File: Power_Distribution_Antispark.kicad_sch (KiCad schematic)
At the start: 88 parts, among them J1 STM Signal Conn, J5 +48V Battery Conn, J6 Motor Conn, Q1 BUK9M42-60EX, Q2 G20P06K, Q3 BUK9M42-60EX, Q4 G20P06K, U1 74LVC1G14GW_125, U2 TPP60308-ES1R-S, U3 TPP60308-ES1R-S, U4 LM331AU-S5TR, U5 TLV74033PDBVR, U8 INA181A3IDBVR

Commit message: final schematic
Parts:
- added R29: 1.1K, Resistor_SMD:R_0201_0603Metric, symbol Device:R_Small_US
- added R30: 1.3K, Resistor_SMD:R_0201_0603Metric, symbol Device:R_Small_US
- R15: value DTO025C100R0JTE3 -> TPAL0263F100RK9; footprint CustomFootprintLibrary:RES_DTO025_VIS -> Package_TO_SOT_SMD:TO-263-3_TabPin4
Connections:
- net GND: now also R30.2
- net PreChargeSense: no longer R32.1
- net PreChargeSenseEnd: now also R29.1, R30.1; no longer D9.2 (A), R32.2
- net at R15.2, R16.2, R33.2: now also R32.1
- new net: D9.2 (A), R29.2, R32.2
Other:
- note added: "I = 0.5A"
- moved on the sheet: R33, R34

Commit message: final schematic
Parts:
- removed C15: 47uF, Capacitor_SMD:C_0201_0603Metric, symbol Device:C_Small
- removed C22, C27: 1uF, Capacitor_SMD:C_0201_0603Metric, symbol Device:C_Small
- removed C3: 2.2uF, Capacitor_SMD:C_0805_2012Metric, symbol Device:C_Small
- removed C8: 39pF, Capacitor_SMD:C_0201_0603Metric, symbol Device:C_Small
- removed R11, R23, R29: 1.1K, Resistor_SMD:R_0201_0603Metric, symbol Device:R_Small_US
- removed R13: 10K, Resistor_SMD:R_0201_0603Metric, symbol Device:R_Small_US
- removed R34: 1.3K, Resistor_SMD:R_0201_0603Metric, symbol Device:R_Small_US
- added C18: 47uF, Capacitor_SMD:C_1206_3216Metric, symbol Device:C_Small
- added C21, C7: 100nF, Capacitor_SMD:C_0603_1608Metric, symbol Device:C_Small
- added C23: 1uF, Capacitor_SMD:C_0603_1608Metric, symbol Device:C_Small
- added C5: 2.2uF, Capacitor_SMD:C_0603_1608Metric, symbol Device:C_Small
- added R15, R20: 2.2K, Resistor_SMD:R_0603_1608Metric, symbol Device:R_Small_US
- added R22: 11K, Resistor_SMD:R_0603_1608Metric, symbol Device:R_Small_US
- added R31: 13K, Resistor_SMD:R_0603_1608Metric, symbol Device:R_Small_US
- added R47: 20K, Resistor_SMD:R_0603_1608Metric, symbol Device:R_Small_US
- C1: renamed from C20; footprint Capacitor_SMD:C_0201_0603Metric -> Capacitor_SMD:C_0603_1608Metric
- C10: value 6.8nF -> 39pF; footprint Capacitor_SMD:C_0201_0603Metric -> Capacitor_SMD:C_0603_1608Metric
- C11: renamed from C7; footprint Capacitor_SMD:C_0201_0603Metric -> Capacitor_SMD:C_0603_1608Metric
- C12: value 100nF -> 6.8nF; footprint Capacitor_SMD:C_0201_0603Metric -> Capacitor_SMD:C_0603_1608Metric
- C13: renamed from C9; footprint Capacitor_SMD:C_0201_0603Metric -> Capacitor_SMD:C_0603_1608Metric
- C14: value 47uF -> 100nF; footprint Capacitor_SMD:C_0201_0603Metric -> Capacitor_SMD:C_0603_1608Metric
- C15: renamed from C11; footprint Capacitor_SMD:C_0201_0603Metric -> Capacitor_SMD:C_0603_1608Metric
- C16: footprint Capacitor_SMD:C_0201_0603Metric -> Capacitor_SMD:C_1206_3216Metric
- C17: renamed from C13; footprint Capacitor_SMD:C_0201_0603Metric -> Capacitor_SMD:C_1206_3216Metric
- C19: value 100nF -> 47uF; footprint Capacitor_SMD:C_0201_0603Metric -> Capacitor_SMD:C_1206_3216Metric
- C2, C4: footprint Capacitor_SMD:C_0805_2012Metric -> Capacitor_SMD:C_0603_1608Metric
- C20: renamed from C17; footprint Capacitor_SMD:C_0201_0603Metric -> Capacitor_SMD:C_0603_1608Metric
- C22: renamed from C18; footprint Capacitor_SMD:C_0201_0603Metric -> Capacitor_SMD:C_0603_1608Metric
- C3: renamed from C1; footprint Capacitor_SMD:C_0805_2012Metric -> Capacitor_SMD:C_0603_1608Metric
- C6: value 100nF -> 1uF; footprint Capacitor_SMD:C_0201_0603Metric -> Capacitor_SMD:C_0603_1608Metric
- C8: renamed from C5; footprint Capacitor_SMD:C_0201_0603Metric -> Capacitor_SMD:C_0603_1608Metric
- C9: renamed from C24; footprint Capacitor_SMD:C_0201_0603Metric -> Capacitor_SMD:C_0603_1608Metric
- R1, R2, R3, R4: footprint Resistor_SMD:R_0201_0603Metric -> Resistor_SMD:R_0603_1608Metric
- R10: renamed from R5; footprint Resistor_SMD:R_0201_0603Metric -> Resistor_SMD:R_0603_1608Metric
- R11: renamed from R8; footprint Resistor_SMD:R_0201_0603Metric -> Resistor_SMD:R_0603_1608Metric
- R12: renamed from R7; footprint Resistor_SMD:R_0201_0603Metric -> Resistor_SMD:R_0603_1608Metric
- R13: renamed from R9; footprint Resistor_SMD:R_0201_0603Metric -> Resistor_SMD:R_0603_1608Metric
- R14: renamed from R10; footprint Resistor_SMD:R_0201_0603Metric -> Resistor_SMD:R_0603_1608Metric
- R16: value 10K -> 20K; footprint Resistor_SMD:R_0201_0603Metric -> Resistor_SMD:R_0603_1608Metric
- R17: renamed from R14; footprint Resistor_SMD:R_0201_0603Metric -> Resistor_SMD:R_0603_1608Metric
- R18: renamed from R12; footprint Resistor_SMD:R_0201_0603Metric -> Resistor_SMD:R_0603_1608Metric
- R19: renamed from R15; footprint Package_TO_SOT_SMD:TO-263-3_TabPin4 -> Package_TO_SOT_SMD:TO-263-2
- R23: renamed from R33; value 1.1K -> 11K; footprint Resistor_SMD:R_0201_0603Metric -> Resistor_SMD:R_0603_1608Metric
- R24: renamed from R20; footprint Resistor_SMD:R_0201_0603Metric -> Resistor_SMD:R_0603_1608Metric
- R25: renamed from R21; footprint Resistor_SMD:R_0201_0603Metric -> Resistor_SMD:R_0603_1608Metric
- R26: renamed from R22; footprint Resistor_SMD:R_0201_0603Metric -> Resistor_SMD:R_0603_1608Metric
- R27: renamed from R17; footprint Resistor_SMD:R_0201_0603Metric -> Resistor_SMD:R_0603_1608Metric
- R28: renamed from R18; footprint Resistor_SMD:R_0201_0603Metric -> Resistor_SMD:R_0603_1608Metric
- R29: renamed from R19; footprint Resistor_SMD:R_0201_0603Metric -> Resistor_SMD:R_0603_1608Metric
- R30: value 1.3K -> 13K; footprint Resistor_SMD:R_0201_0603Metric -> Resistor_SMD:R_0603_1608Metric
- R33: renamed from R24; footprint Resistor_SMD:R_0201_0603Metric -> Resistor_SMD:R_0603_1608Metric
- R34: renamed from R31; footprint Resistor_SMD:R_0201_0603Metric -> Resistor_SMD:R_0603_1608Metric
- R35: renamed from R27; footprint Resistor_SMD:R_0201_0603Metric -> Resistor_SMD:R_0603_1608Metric
- R36: renamed from R28; footprint Resistor_SMD:R_0201_0603Metric -> Resistor_SMD:R_0603_1608Metric
- R37: renamed from R25; footprint Resistor_SMD:R_0201_0603Metric -> Resistor_SMD:R_0603_1608Metric
- R38: renamed from R26; footprint Resistor_SMD:R_0201_0603Metric -> Resistor_SMD:R_0603_1608Metric
- R5: renamed from R36; footprint Resistor_SMD:R_0201_0603Metric -> Resistor_SMD:R_0603_1608Metric
- R6: renamed from R46; footprint Resistor_SMD:R_0201_0603Metric -> Resistor_SMD:R_0603_1608Metric
- R7: renamed from R35; footprint Resistor_SMD:R_0201_0603Metric -> Resistor_SMD:R_0603_1608Metric
- R8: renamed from R45; footprint Resistor_SMD:R_0201_0603Metric -> Resistor_SMD:R_0603_1608Metric
- R9: renamed from R6; footprint Resistor_SMD:R_0201_0603Metric -> Resistor_SMD:R_0603_1608Metric
- renumbered D2 to D1, D7 to D10, D9 to D11, D1 to D2, D12 to D3, D3 to D5, D5 to D6, D6 to D7, D13 to D8, D8 to D9, J5 to J2, J6 to J3, L2 to L1, L1 to L2, R32 to R21, U5 to U1, U1 to U2, U2 to U4, U4 to U5, U8 to U6
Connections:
- net +12V: now also C19.1
- net +3V3: now also C6.1
- net +5V: now also C18.1, C23.1; no longer C14.1, C6.1, C8.1, R5.1, R6.1, R7.1, R8.1, U3.3 (EN), U4.3 (EN)
- net GND: now also C12.2, C18.2, C21.2, C23.2, C5.2, C7.2, R15.1, R20.1, R31.2; no longer C14.2, C2.2
- net PreChargeSense: now also R30.1
- net PreChargeSenseEnd: now also R22.1, R31.1; no longer R30.1
- net V_S_5V_Output: now also C21.1; no longer C19.1
- net at U5.1 (IN-): now also R15.2, R47.2
- net at R9.1, U3.6 (COMP): now also C10.1
- net at R9.2: now also C12.1; no longer C10.1
- net at R21.1, R23.2: now also R16.1, R19.3; no longer R16.2, R19.2
- net at D9.1 (K), L1.1, U3.8 (SW): now also C14.1; no longer C12.1
- net at R17.2: now also C14.2; no longer C12.2
- net at C3.1, F2.2, R8.2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: now also C4.1
- net at R33.1, U5.3 (IN+): now also R16.2, R20.2; no longer R16.1
- net at Q4.2 (D), R19.1: now also R47.1
- net at F3.2, R7.2, U3.2 (VIN): now also C5.1; no longer C2.1, C4.1
- net at D11.2 (A), R21.2: now also R22.2
- net C_Sense_12V1 renamed C_Sense_12V_1
- net C_Sense_12V2 renamed C_Sense_12V_2
- net C_Sense_12V3 renamed C_Sense_12V_3
- net C_Sense_5V1 renamed C_Sense_5V_1
- net C_Sense_5V2 renamed C_Sense_5V_2
- net C_Sense_5V3 renamed C_Sense_5V_3
- new net: C8.1, R6.1, R8.1, U4.3 (EN)
- new net: C7.1, R5.1, R7.1, U3.3 (EN)

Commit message: final schematic
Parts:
- R5, R6: value 1.5K -> 3K
- R7, R8: value 10.5K -> 21K
- renumbered C3 to C2, C2 to C3, R47 to R16, R16 to R20, R20 to R30, R30 to R31, R31 to R32
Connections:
- net GND: now also C3.2
- net at C3.1: now also C5.1, F3.2, R7.2, U3.2 (VIN)

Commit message: damir review
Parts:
- removed D6: MBRD20100, Package_TO_SOT_SMD:TO-252-3_TabPin2, symbol Diode:1N4148WT
- removed R22, R23: 11K, Resistor_SMD:R_0603_1608Metric, symbol Device:R_Small_US
- removed R31, R32: 13K, Resistor_SMD:R_0603_1608Metric, symbol Device:R_Small_US
- added H1, H2: MountingHole, MountingHole:MountingHole_2.5mm, symbol Mechanical:MountingHole
- R16: value 20K -> 22K
- R33: value 10K -> 402K
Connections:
- net PreChargeSenseEnd is gone; now on net GND: U6.4 (IN-)
- net +48V: no longer J3.1 (P)
- net GND: now also R21.2; no longer J3.2 (N), J3.SH1 (SHIELD), J3.SH2 (SHIELD)
- net MotorConn: now also J3.1 (P)
- net at F1.2: now also D3.1 (K), D7.1 (K), D8.1 (K), Q2.3 (S), Q4.3 (S), R13.1, R4.1
- net at R19.3, R20.1: now also D11.2 (A); no longer R21.1
- net PreChargeSense: no longer names the net of U6.3 (IN+)
- net PreChargeSense: now also J3.2 (N), J3.SH1 (SHIELD), J3.SH2 (SHIELD), R21.1
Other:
- moved on the sheet: C23, D11, F1, J2, J3, R21, U6

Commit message: final schematic
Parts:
- F1: footprint CustomFootprintLibrary:FUSC6125X279N-0679L9150-05 -> CustomFootprintLibrary:FUSE_0679L9200-05_BEL
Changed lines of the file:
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@@
 			)
 		)
-		(property "Footprint" "CustomFootprintLibrary:FUSC6125X279N-0679L9150-05"
+		(property "Footprint" "CustomFootprintLibrary:FUSE_0679L9200-05_BEL"
 			(at 55.88 39.37 0)
 			(effects
@@
 			)
 		)
-		(property "Datasheet" "https://www.digikey.ca/en/products/detail/bel-fuse-inc/0679L9150-05/5844044"
+		(property "Datasheet" "https://www.digikey.ca/en/products/detail/bel-fuse-inc/0679L9200-05/5844045?s=N4IgTCBcDaIAwDYDsBOAMisc4Fo4FYQBdAXyA"
 			(at 55.88 39.37 0)
 			(effects
@@
 			)
 		)
-		(property "Description" "FUSE BRD MNT 15A 125VAC/VDC 2SMD"
+		(property "Description" "FUSE BRD MNT 20A 125VAC/VDC 2SMD"
 			(at 55.88 39.37 0)
 			(effects

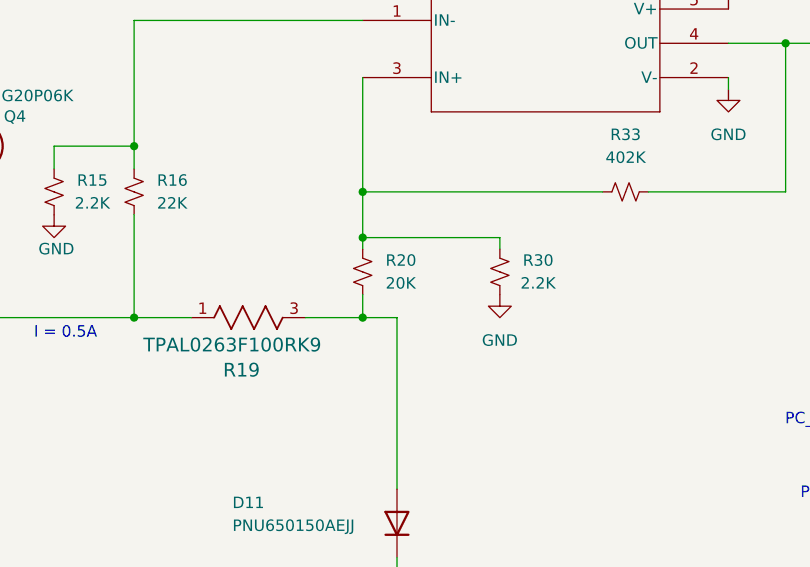
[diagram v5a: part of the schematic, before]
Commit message: tweaked comparator resistor values
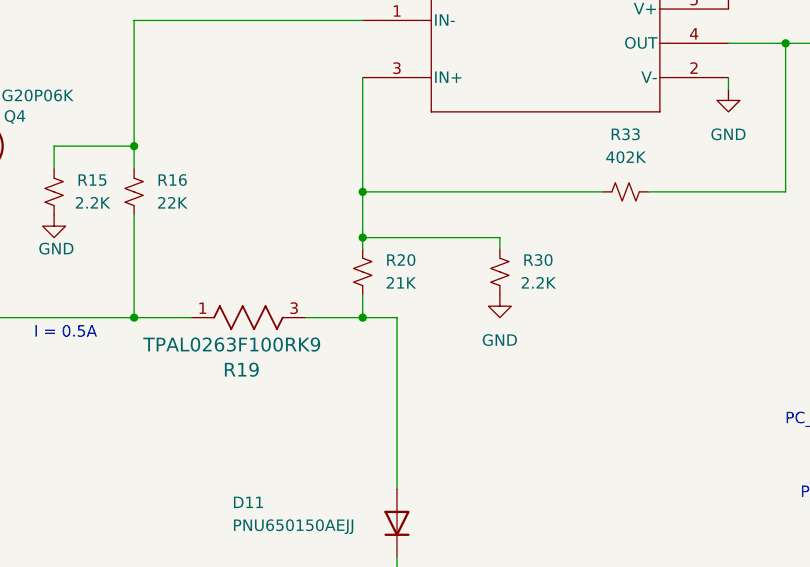
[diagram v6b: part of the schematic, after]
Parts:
- R20: value 20K -> 21K
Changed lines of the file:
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@@
 			)
 		)
-		(property "Value" "20K"
+		(property "Value" "21K"
 			(at 193.04 67.3099 0)
 			(effects
@@
 			)
 		)
-		(property "Datasheet" "https://www.digikey.ca/en/products/detail/stackpole-electronics-inc/RNCF0603BTE20K0/2027042"
+		(property "Datasheet" "https://www.digikey.ca/en/products/detail/stackpole-electronics-inc/RMCF0603FT21K0/1713784"
 			(at 190.5 66.04 0)
 			(effects
@@
 			)
 		)
-		(property "Description" "RES SMD 20K OHM 0.1% 1/6W 0603"
+		(property "Description" "RES 21K OHM 1% 1/10W 0603"
 			(at 190.5 66.04 0)
 			(effects

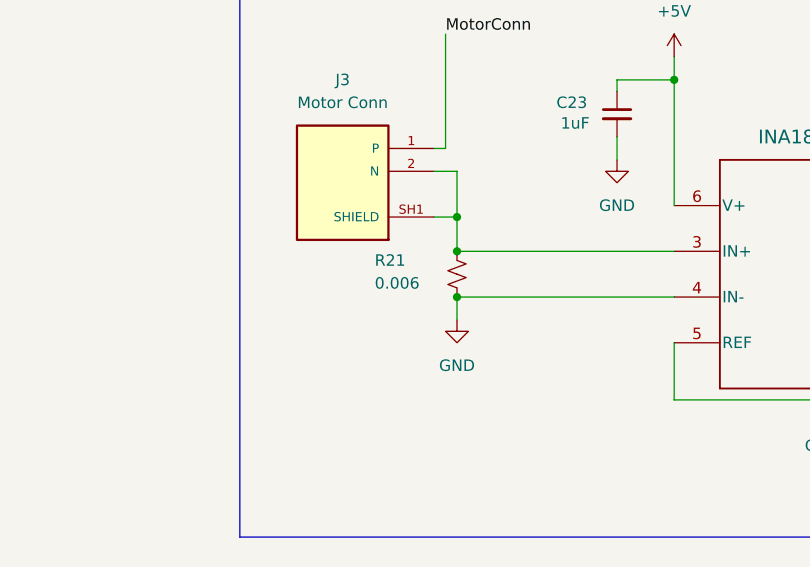
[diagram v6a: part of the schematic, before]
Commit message: tweaked comparator values and shunt
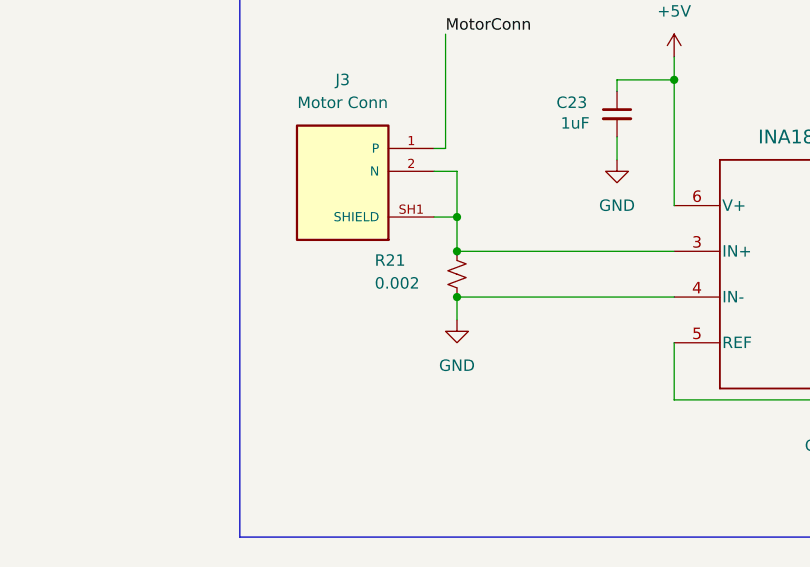
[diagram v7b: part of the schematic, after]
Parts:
- C2, C3, C4, C5: footprint Capacitor_SMD:C_0603_1608Metric -> Capacitor_SMD:C_1206_3216Metric
- R21: value 0.006 -> 0.002

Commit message: minor component datasheet fix + layout started
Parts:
- J1: footprint CustomFootprintLibrary:ADAM_PH2-08-UA -> CustomFootprintLibrary:ADAM_2PH2-16-UA
- L1: footprint (none) -> CustomFootprintLibrary:IND_MGAH06036R8M-10
- U3, U4: footprint CustomFootprintLibrary:TPP60308-ES1R-S -> CustomFootprintLibrary:ES1ESOP-8-F_TPK
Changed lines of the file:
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@@
 			)
 		)
-		(property "Footprint" "CustomFootprintLibrary:ADAM_PH2-08-UA"
+		(property "Footprint" "CustomFootprintLibrary:ADAM_2PH2-16-UA"
 			(at 59.69 351.79 0)
 			(effects
@@
 			)
 		)
-		(property "Datasheet" "https://www.digikey.ca/en/products/detail/adam-tech/PH2-08-UA/9830443"
+		(property "Datasheet" "https://www.digikey.ca/en/products/detail/adam-tech/2PH2-16-UA/9830539"
 			(at 59.69 351.79 0)
 			(effects
@@
 			)
 		)
-		(property "Description" "CONN HEADER VERT 8POS 2.54MM"
+		(property "Description" "CONN HEADER VERT 16POS 2MM"
 			(at 59.69 351.79 0)
 			(effects
@@
 			)
 		)
-		(property "Footprint" "CustomFootprintLibrary:TPP60308-ES1R-S"
+		(property "Footprint" "CustomFootprintLibrary:ES1ESOP-8-F_TPK"
 			(at 130.81 217.17 0)
 			(effects
@@
 			)
 		)
-		(property "Footprint" "CustomFootprintLibrary:TPP60308-ES1R-S"
+		(property "Footprint" "CustomFootprintLibrary:ES1ESOP-8-F_TPK"
 			(at 132.08 143.51 0)
 			(effects
@@
 			)
 		)
-		(property "Footprint" ""
+		(property "Footprint" "CustomFootprintLibrary:IND_MGAH06036R8M-10"
 			(at 194.31 215.9 0)
 			(effects
@@
 					(size 1.27 1.27)
 				)
+				(hide yes)
 			)
 		)
